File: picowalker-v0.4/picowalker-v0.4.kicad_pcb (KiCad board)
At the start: 4 copper layers, 47.4 x 50.5 mm, 97 parts, among them IC1 RT6150B-33GQW, J1 12402012E212A, J2 BAT, J3 SWD, J4 UART, SW1 ~{BOOT}, SW2 RUN, SW3 BUT_M, SW4 BUT_R, SW5 BUT_L, U1 RP2350A-QFN60, U2 W25Q128JVP, U3 BMA400, U4 M95512DxMC, U5 TFBS4711, U6 BQ25628ERYKR, U7 DO0180FMST0x, U8 DT1240-04LP-7, Y1 ABM8-272-T3, Y2 SIT1533AI-H4-DCC-32.768E

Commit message: v0.4: idk, minimal changes
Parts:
- removed IC1: RT6150B-33GQW, picowalker:SON50P250X250X80-11N-D
- added U9: RT6150B-33GQW, picowalker:SON50P250X250X80-11N-D, F.Cu at (157.7, 86.7)
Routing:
- net GND: track 67.5 -> 68.3 mm

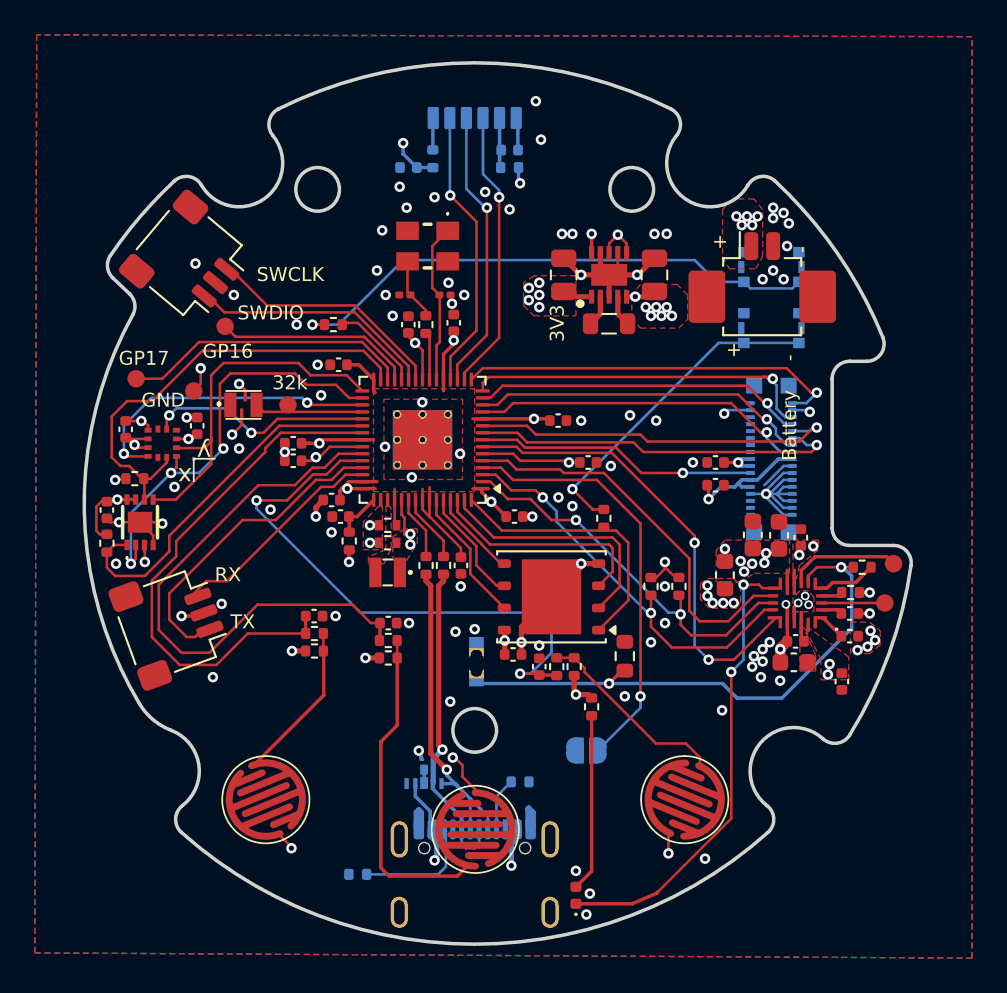
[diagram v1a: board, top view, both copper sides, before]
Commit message: v0.4: add huawei speaker
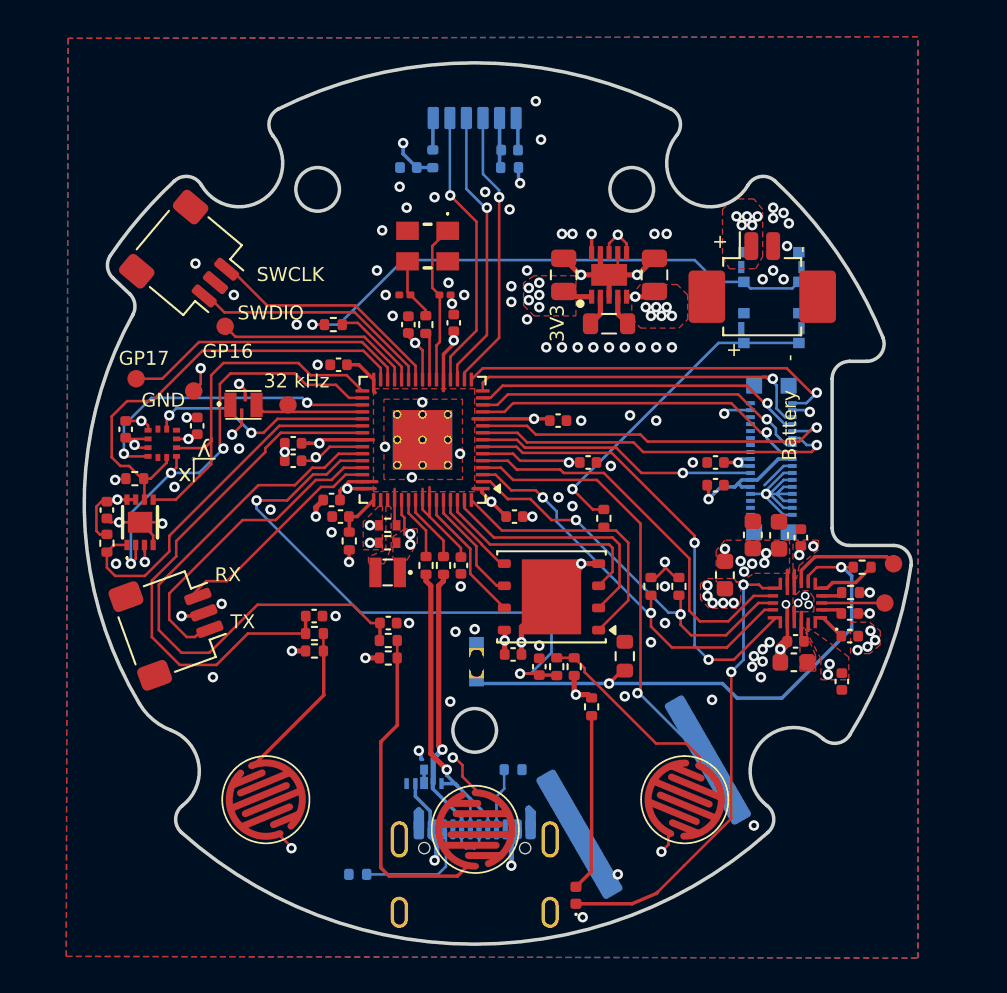
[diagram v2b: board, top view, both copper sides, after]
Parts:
- BZ1: footprint Jumper:SolderJumper-2_P1.3mm_Open_RoundedPad1.0x1.5mm -> picowalker:Huawei_P20_Speaker
- moved BZ1 4.23 mm to (159.7, 116.6), turned to 120 degrees
- moved R7 0.81 mm to (152.2, 115.0)
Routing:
- net /SOUND: track 24.4 -> 25.9 mm
- net /connectors/CC1: track 3.05 -> 3.58 mm
- net GND: track 68.3 -> 68.4 mm, vias 96 -> 106
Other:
- board text added: "32 kHz"
- board text added: "PCB: mamba2410 Shell: Kamp Logo and art: ZenithKnight"
- board text removed: "32k"

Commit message: v0.4: add test points for touch pad
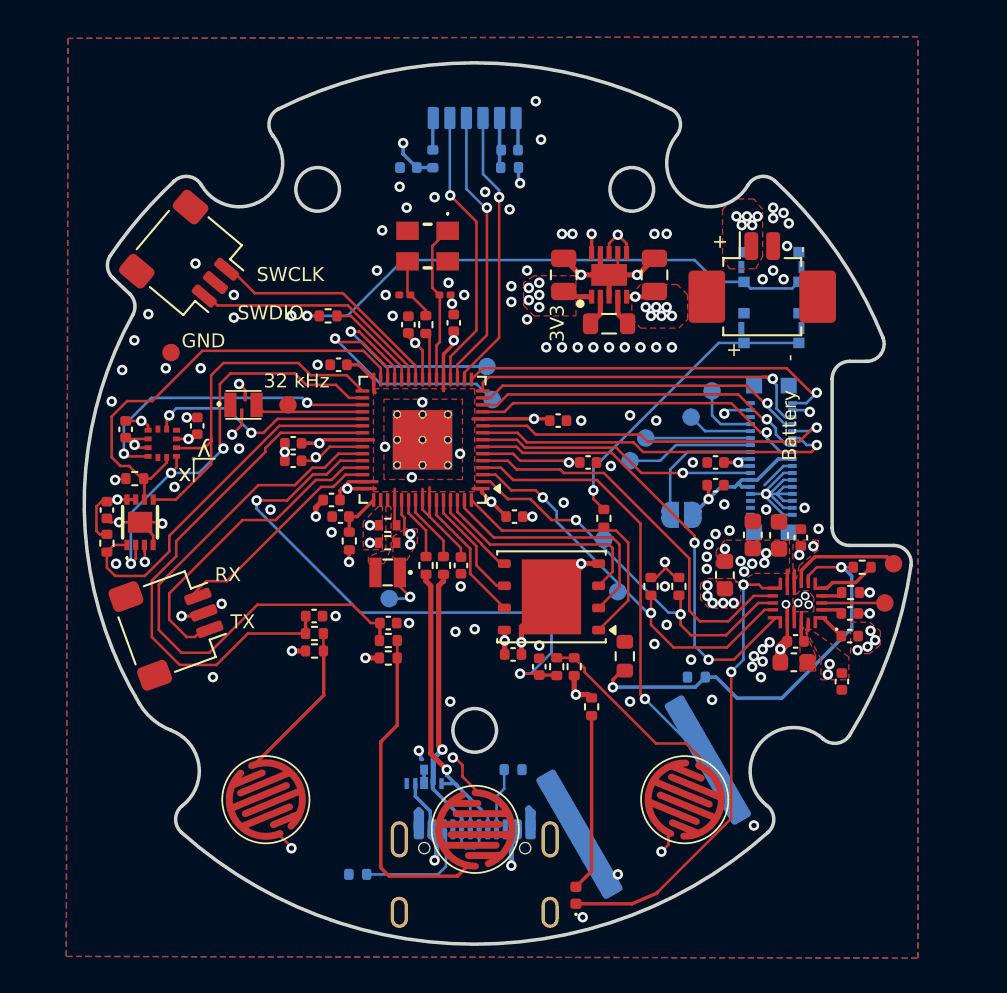
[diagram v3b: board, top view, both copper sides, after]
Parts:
- added JP1: TP_VCC_JMP, Jumper:SolderJumper-2_P1.3mm_Open_RoundedPad1.0x1.5mm, B.Cu at (161.8, 100.4)
- added TP10: TP_SCL, picowalker:TestPoint_Pad_D1.0mm_Nosilk, B.Cu at (163.6, 93.3)
- added TP11: TP_SDA, picowalker:TestPoint_Pad_D1.0mm_Nosilk, B.Cu at (162.4, 94.8)
- added TP12: 1V1, picowalker:TestPoint_Pad_D1.0mm_Nosilk, B.Cu at (145.1, 105.2)
- added TP13: SCL, picowalker:TestPoint_Pad_D1.0mm_Nosilk, B.Cu at (158.2, 104.8)
- added TP5: SDA, picowalker:TestPoint_Pad_D1.0mm_Nosilk, B.Cu at (157.4, 101.8)
- added TP8: TP_INT, picowalker:TestPoint_Pad_D1.0mm_Nosilk, B.Cu at (159.8, 96.0)
- added TP9: TP_RESET, picowalker:TestPoint_Pad_D1.0mm_Nosilk, B.Cu at (158.9, 97.3)
- TH1: footprint picowalker:R_0402_1005Metric_Sunken -> Resistor_SMD:R_0402_1005Metric
- TP6, TP7: moved to B.Cu
- moved TP7 20.4 mm to (151.0, 93.8), turned to 180 degrees
- moved TP6 15.2 mm to (150.7, 91.9), turned to 180 degrees
- moved TH1 12.6 mm to (162.7, 109.7), turned to 180 degrees
- moved TP4 2.56 mm to (132.6, 91.1)
- moved R2 0.58 mm to (141.6, 89.0)
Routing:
- net /screen/TP_VCC: track 0.00 -> 7.61 mm
- net /TP_RESET: track 0.00 -> 7.27 mm
- net /power/TS: track 31.5 -> 24.5 mm
- net /TP_INT: track 0.00 -> 6.00 mm
- net /screen/TP_I2C.SCL: track 0.00 -> 3.81 mm
- net /screen/TP_I2C.SDA: track 0.00 -> 3.73 mm
- net +1.1V: track 32.3 -> 35.2 mm, vias 9 -> 10
- net /mcu/GP17: track 16.6 -> 14.9 mm, vias 0 -> 1
- net GND: track 68.4 -> 66.9 mm, vias 106 -> 121
- net /mcu/~{BOOT}: track 18.7 -> 17.4 mm
- net /mcu/GP16: track 11.4 -> 12.7 mm, vias 0 -> 1
- net +3.3V: track 62.2 -> 63.4 mm
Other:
- board text added: "1V1"
- board text added: "SCL"
- board text added: "SDA"
- board text added: "TP_INT"
- board text added: "TP_RESET"
- board text added: "TP_SCL"
- board text added: "TP_SDA"
- board text added: "TP_VCC"

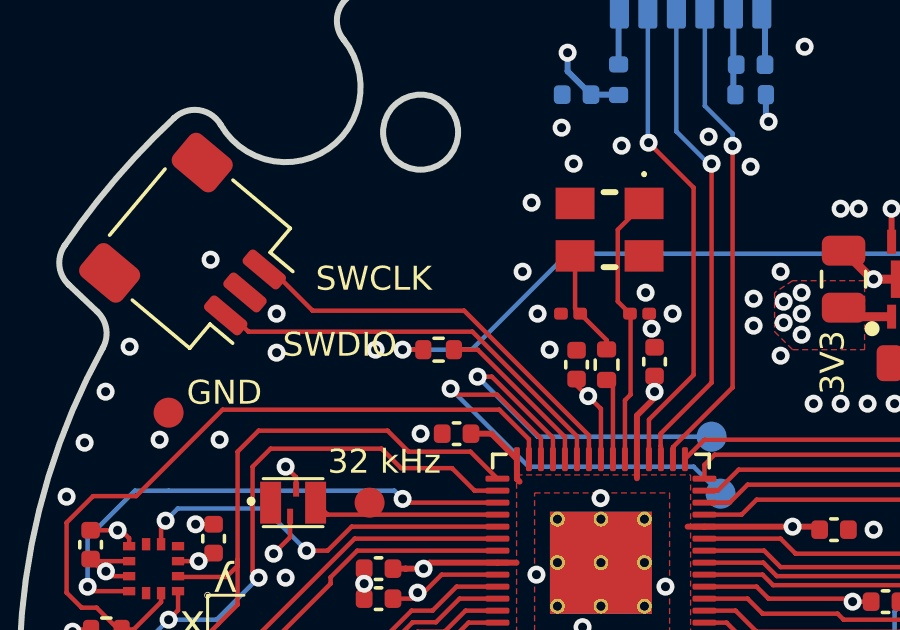
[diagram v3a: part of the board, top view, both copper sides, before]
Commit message: v0.4: change xtal caps to 0402
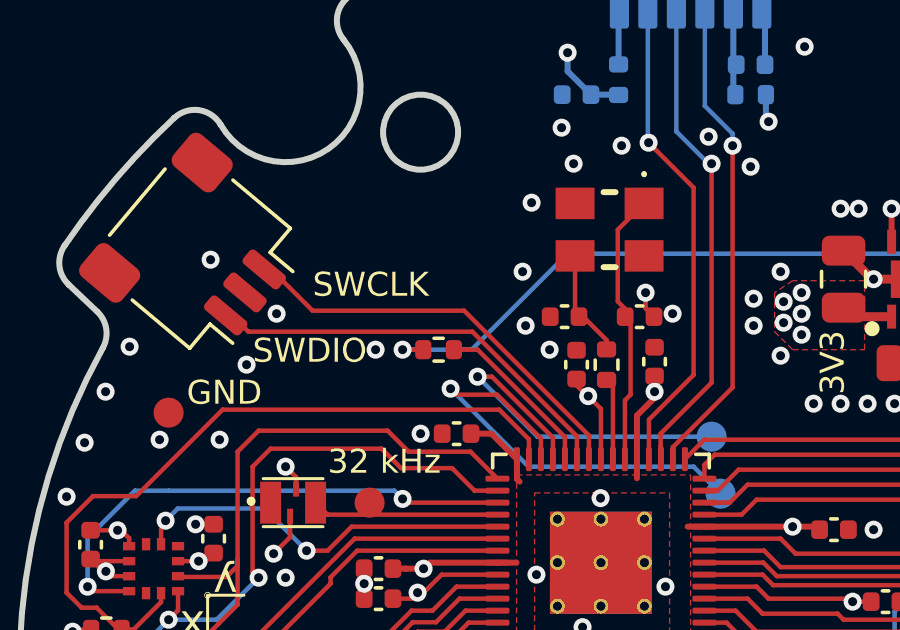
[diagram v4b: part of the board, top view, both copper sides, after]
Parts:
- C2, C4: footprint Capacitor_SMD:C_0201_0603Metric -> Capacitor_SMD:C_0402_1005Metric
- moved C4 0.22 mm to (145.8, 87.9)
- moved C2 0.10 mm to (148.3, 87.9)
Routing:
- net GND: track 66.9 -> 67.8 mm, vias 121 -> 120
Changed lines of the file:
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@@
 		(embedded_fonts no)
 	)
-	(footprint "Capacitor_SMD:C_0201_0603Metric"
+	(footprint "Capacitor_SMD:C_0402_1005Metric"
 		(layer "F.Cu")
-		(at 145.999 87.799 180)
-		(descr "Capacitor SMD 0201 (0603 Metric), square (rectangular) end terminal, IPC-7351 nominal, (Body size source: https://www.vishay.com/docs/20052/crcw0201e3.pdf), generated with kicad-footprint-generator")
+		(at 145.8 87.9 180)
+		(descr "Capacitor SMD 0402 (1005 Metric), square (rectangular) end terminal, IPC-7351 nominal, (Body size source: IPC-SM-782 page 76, https://www.pcb-3d.com/wordpress/wp-content/uploads/ipc-sm-782a_amendment_1_and_2.pdf), generated with kicad-footprint-generator")
 		(tags "capacitor")
 		(property "Reference" "C4"
-			(at 0 -1.05 0)
+			(at 0 -1.16 180)
 			(layer "F.SilkS")
 			(hide yes)
@@
 		)
 		(property "Value" "15p"
-			(at 0 1.05 0)
+			(at 0 1.16 180)
 			(layer "F.Fab")
 			(effects
@@
 		)
 		(property "Datasheet" "~"
-			(at 0 0 0)
+			(at 0 0 180)
 			(layer "F.Fab")
 			(hide yes)
@@
 		)
 		(property "Description" "Unpolarized capacitor"
-			(at 0 0 0)
+			(at 0 0 180)
 			(layer "F.Fab")
 			(hide yes)
@@
 		(attr smd)
 		(fp_line
-			(start 0.7 0.35)
-			(end -0.7 0.35)
-			(stroke
-				(width 0.05)
-				(type solid)
-			)
-			(layer "F.CrtYd")
-		)
-		(fp_line
-			(start 0.7 -0.35)
-			(end 0.7 0.35)
+			(start -0.107836 0.36)
+			(end 0.107836 0.36)
 			(stroke
-				(width 0.05)
+				(width 0.12)
 				(type solid)
 			)
-			(layer "F.CrtYd")
+			(layer "F.SilkS")
 		)
 		(fp_line
-			(start -0.7 0.35)
-			(end -0.7 -0.35)
+			(start -0.107836 -0.36)
+			(end 0.107836 -0.36)
 			(stroke
-				(width 0.05)
+				(width 0.12)
 				(type solid)
 			)
-			(layer "F.CrtYd")
+			(layer "F.SilkS")
 		)
-		(fp_line
-			(start -0.7 -0.35)
-			(end 0.7 -0.35)
+		(fp_rect
+			(start -0.91 -0.46)
+			(end 0.91 0.46)
 			(stroke
 				(width 0.05)
 				(type solid)
 			)
+			(fill no)
 			(layer "F.CrtYd")
 		)
-		(fp_line
-			(start 0.3 0.15)
-			(end -0.3 0.15)
-			(stroke
-				(width 0.1)
-				(type solid)
-			)
-			(layer "F.Fab")
-		)
-		(fp_line
-			(start 0.3 -0.15)
-			(end 0.3 0.15)
-			(stroke
-				(width 0.1)
-				(type solid)
-			)
-			(layer "F.Fab")
-		)
-		(fp_line
-			(start -0.3 0.15)
-			(end -0.3 -0.15)
-			(stroke
-				(width 0.1)
-				(type solid)
-			)
-			(layer "F.Fab")
-		)
-		(fp_line
-			(start -0.3 -0.15)
-			(end 0.3 -0.15)
+		(fp_rect
+			(start -0.5 -0.25)
+			(end 0.5 0.25)
 			(stroke
 				(width 0.1)
 				(type solid)
 			)
+			(fill no)
 			(layer "F.Fab")
 		)
 		(fp_text user "${REFERENCE}"
-			(at 0 -0.68 0)
+			(at 0 0 180)
 			(layer "F.Fab")
 			(effects
@@
 			)
 		)
-		(pad "" smd roundrect
-			(at -0.345 0 180)
-			(size 0.318 0.36)
-			(layers "F.Paste")
-			(roundrect_rratio 0.25)
-		)
-		(pad "" smd roundrect
-			(at 0.345 0 180)
-			(size 0.318 0.36)
-			(layers "F.Paste")
-			(roundrect_rratio 0.25)
-		)
 		(pad "1" smd roundrect
-			(at -0.32 0 180)
-			(size 0.46 0.4)
-			(layers "F.Cu" "F.Mask")
+			(at -0.48 0 180)
+			(size 0.56 0.62)
+			(layers "F.Cu" "F.Mask" "F.Paste")
 			(roundrect_rratio 0.25)
 			(net 5 "Net-(C4-Pad1)")
@@
 		)
 		(pad "2" smd roundrect
-			(at 0.32 0 180)
-			(size 0.46 0.4)
-			(layers "F.Cu" "F.Mask")
+			(at 0.48 0 180)
+			(size 0.56 0.62)
+			(layers "F.Cu" "F.Mask" "F.Paste")
 			(roundrect_rratio 0.25)
 			(net 1 "GND")
@@
 		)
 		(embedded_fonts no)
-		(model "${KICAD9_3DMODEL_DIR}/Capacitor_SMD.3dshapes/C_0201_0603Metric.step"
+		(model "${KICAD9_3DMODEL_DIR}/Capacitor_SMD.3dshapes/C_0402_1005Metric.step"
 			(offset
 				(xyz 0 0 0)
@@
 		)
 	)
-	(footprint "Capacitor_SMD:C_0201_0603Metric"
+	(footprint "Capacitor_SMD:C_0402_1005Metric"
 		(layer "F.Cu")
-		(at 148.299 87.799)
-		(descr "Capacitor SMD 0201 (0603 Metric), square (rectangular) end terminal, IPC-7351 nominal, (Body size source: https://www.vishay.com/docs/20052/crcw0201e3.pdf), generated with kicad-footprint-generator")
+		(at 148.3 87.9)
+		(descr "Capacitor SMD 0402 (1005 Metric), square (rectangular) end terminal, IPC-7351 nominal, (Body size source: IPC-SM-782 page 76, https://www.pcb-3d.com/wordpress/wp-content/uploads/ipc-sm-782a_amendment_1_and_2.pdf), generated with kicad-footprint-generator")
 		(tags "capacitor")
 		(property "Reference" "C2"
-			(at 0 -1.05 0)
+			(at 0 -1.16 0)
 			(layer "F.SilkS")
 			(hide yes)
@@
 		)
 		(property "Value" "15p"
-			(at 0 1.05 0)
+			(at 0 1.16 0)
 			(layer "F.Fab")
 			(effects
@@
 		(attr smd)
 		(fp_line
-			(start -0.7 -0.35)
-			(end 0.7 -0.35)
-			(stroke
-				(width 0.05)
-				(type solid)
-			)
-			(layer "F.CrtYd")
-		)
-		(fp_line
-			(start -0.7 0.35)
-			(end -0.7 -0.35)
+			(start -0.107836 -0.36)
+			(end 0.107836 -0.36)
 			(stroke
-				(width 0.05)
+				(width 0.12)
 				(type solid)
 			)
-			(layer "F.CrtYd")
+			(layer "F.SilkS")
 		)
 		(fp_line
-			(start 0.7 -0.35)
-			(end 0.7 0.35)
+			(start -0.107836 0.36)
+			(end 0.107836 0.36)
 			(stroke
-				(width 0.05)
+				(width 0.12)
 				(type solid)
 			)
-			(layer "F.CrtYd")
+			(layer "F.SilkS")
 		)
-		(fp_line
-			(start 0.7 0.35)
-			(end -0.7 0.35)
+		(fp_rect
+			(start -0.91 -0.46)
+			(end 0.91 0.46)
 			(stroke
 				(width 0.05)
 				(type solid)
 			)
+			(fill no)
 			(layer "F.CrtYd")
 		)
-		(fp_line
-			(start -0.3 -0.15)
-			(end 0.3 -0.15)
-			(stroke
-				(width 0.1)
-				(type solid)
-			)
-			(layer "F.Fab")
-		)
-		(fp_line
-			(start -0.3 0.15)
-			(end -0.3 -0.15)
-			(stroke
-				(width 0.1)
-				(type solid)
-			)
-			(layer "F.Fab")
-		)
-		(fp_line
-			(start 0.3 -0.15)
-			(end 0.3 0.15)
-			(stroke
-				(width 0.1)
-				(type solid)
-			)
-			(layer "F.Fab")
-		)
-		(fp_line
-			(start 0.3 0.15)
-			(end -0.3 0.15)
+		(fp_rect
+			(start -0.5 -0.25)
+			(end 0.5 0.25)
 			(stroke
 				(width 0.1)
 				(type solid)
 			)
+			(fill no)
 			(layer "F.Fab")
 		)
 		(fp_text user "${REFERENCE}"
-			(at 0 -0.68 0)
+			(at 0 0 0)
 			(layer "F.Fab")
 			(effects
@@
 			)
 		)
-		(pad "" smd roundrect
-			(at -0.345 0)
-			(size 0.318 0.36)
-			(layers "F.Paste")
-			(roundrect_rratio 0.25)
-		)
-		(pad "" smd roundrect
-			(at 0.345 0)
-			(size 0.318 0.36)
-			(layers "F.Paste")
-			(roundrect_rratio 0.25)
-		)
 		(pad "1" smd roundrect
-			(at -0.32 0)
-			(size 0.46 0.4)
-			(layers "F.Cu" "F.Mask")
+			(at -0.48 0)
+			(size 0.56 0.62)
+			(layers "F.Cu" "F.Mask" "F.Paste")
 			(roundrect_rratio 0.25)
 			(net 3 "/mcu/XIN")
@@
 		)
 		(pad "2" smd roundrect
-			(at 0.32 0)
-			(size 0.46 0.4)
-			(layers "F.Cu" "F.Mask")
+			(at 0.48 0)
+			(size 0.56 0.62)
+			(layers "F.Cu" "F.Mask" "F.Paste")
 			(roundrect_rratio 0.25)
 			(net 1 "GND")
@@
 		)
 		(embedded_fonts no)
-		(model "${KICAD9_3DMODEL_DIR}/Capacitor_SMD.3dshapes/C_0201_0603Metric.step"
+		(model "${KICAD9_3DMODEL_DIR}/Capacitor_SMD.3dshapes/C_0402_1005Metric.step"
 			(offset
 				(xyz 0 0 0)
@@
 	)
 	(gr_text "SWDIO"
-		(at 136.4 89.3 0)
+		(at 135.4 89.5 0)
 		(layer "F.SilkS")
 		(effects
@@
 	)
 	(gr_text "SWCLK"
-		(at 137.5 87.1 0)
+		(at 137.4 87.3 0)
 		(layer "F.SilkS")
 		(effects
@@
 	)
 	(segment
+		(start 148.5 87.1)
+		(end 148.5 87.62)
+		(width 0.15)
+		(layer "F.Cu")
+		(net 1)
+	)
+	(segment
 		(start 158.2 85.4)
 		(end 158.2 86.15)
@@
 	)
 	(segment
+		(start 148.5 87.62)
+		(end 148.78 87.9)
+		(width 0.15)
+		(layer "F.Cu")
+		(net 1)
+	)
+	(segment
 		(start 130.17 96.05)
 		(end 130.1 95.98)
@@
 	)
 	(via
-		(at 144.9 87.8)
+		(at 144.5 88.2)
 		(size 0.6)
 		(drill 0.3)
@@
 	)
 	(via
-		(at 148.7 88.3)
-		(size 0.6)
-		(drill 0.3)
-		(layers "F.Cu" "B.Cu")
-		(free yes)
-		(net 1)
-	)
-	(via
 		(at 148.5 87.1)
 		(size 0.6)
@@
 	)
 	(via
-		(at 136.2 89.1)
+		(at 135.2 89.5)
 		(size 0.6)
 		(drill 0.3)
@@
 			"b787ce9c-462f-4f64-9ca9-d9c073ad8d34" "b7b83070-610c-4418-a522-34a5919aaee5"
 			"b7e4027b-0431-4b3b-a7be-759d58256fd6" "b87a65fb-0a04-4904-8134-4a64eb2357b4"
-			"bb7373ac-7416-401a-8b31-e64b855f0e43" "c1ba1bd1-64d1-480a-9d63-ca59ffd28389"
+			"b9db1f77-f94c-460d-8f73-663af5d95edd" "bb7373ac-7416-401a-8b31-e64b855f0e43"
+			"c06c1610-d607-4422-943f-40c246ef228d" "c1ba1bd1-64d1-480a-9d63-ca59ffd28389"
 			"c5091231-45d7-43fa-8e17-fe23beee077d" "ca4ba06e-7f81-4c7a-9bf3-e727e59392c1"
 			"cb61ff23-68f4-45d6-b203-777d1ee5b869" "cf90b12c-cec6-4778-81e0-9b4868390be0"

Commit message: v0.4: send to manufacture
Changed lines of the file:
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@@
 	)
 	(gr_text "Speaker"
-		(at 158.4 111.1 30)
+		(at 158.5 111.3 30)
 		(layer "B.SilkS")
 		(effects
@@
 	)
 	(via
-		(at 130.5 90.4)
-		(size 0.6)
-		(drill 0.3)
+		(at 130.5 90.5)
+		(size 0.6)
+		(drill 0.3)
